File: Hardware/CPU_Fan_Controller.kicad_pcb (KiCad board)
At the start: 2 copper layers, 45.5 x 10.8 mm, 14 parts, among them J1 Conn_01x05_Pin, J2 Conn_01x04_Socket, J3 Conn_01x01_Socket, J4 Conn_01x01_Socket, SW1 SW_Push, U1 STM32G030J6Mx, U2 LD1117S33TR_SOT223

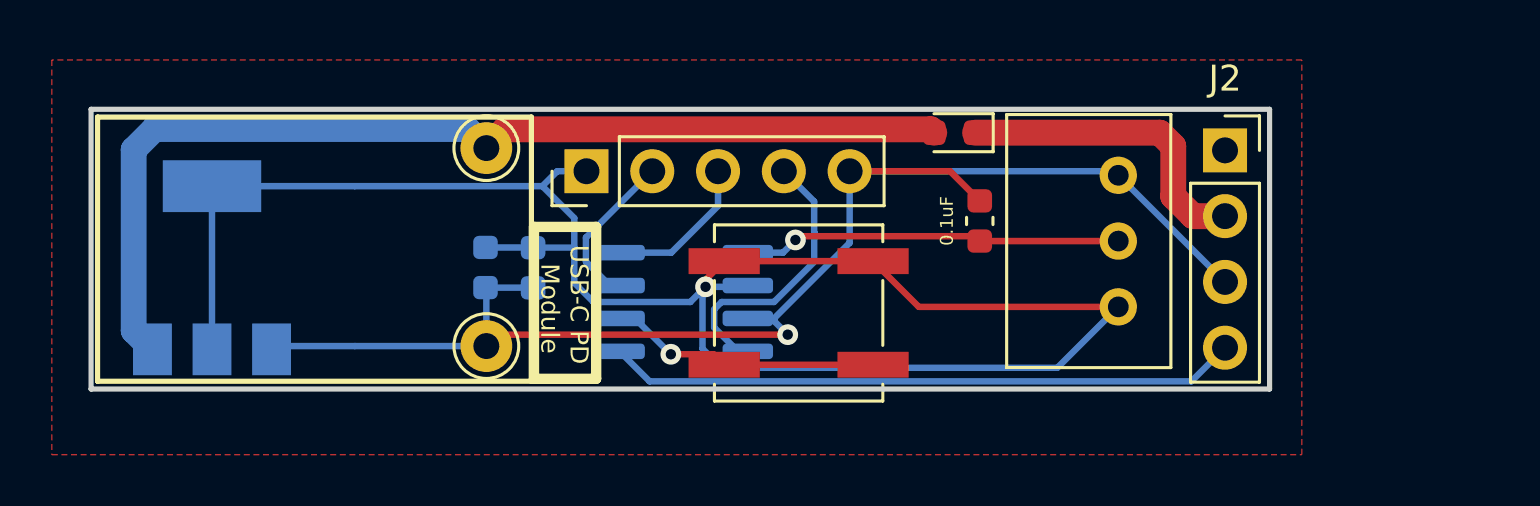
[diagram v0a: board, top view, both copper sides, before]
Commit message: Code is functioning, updated PCB
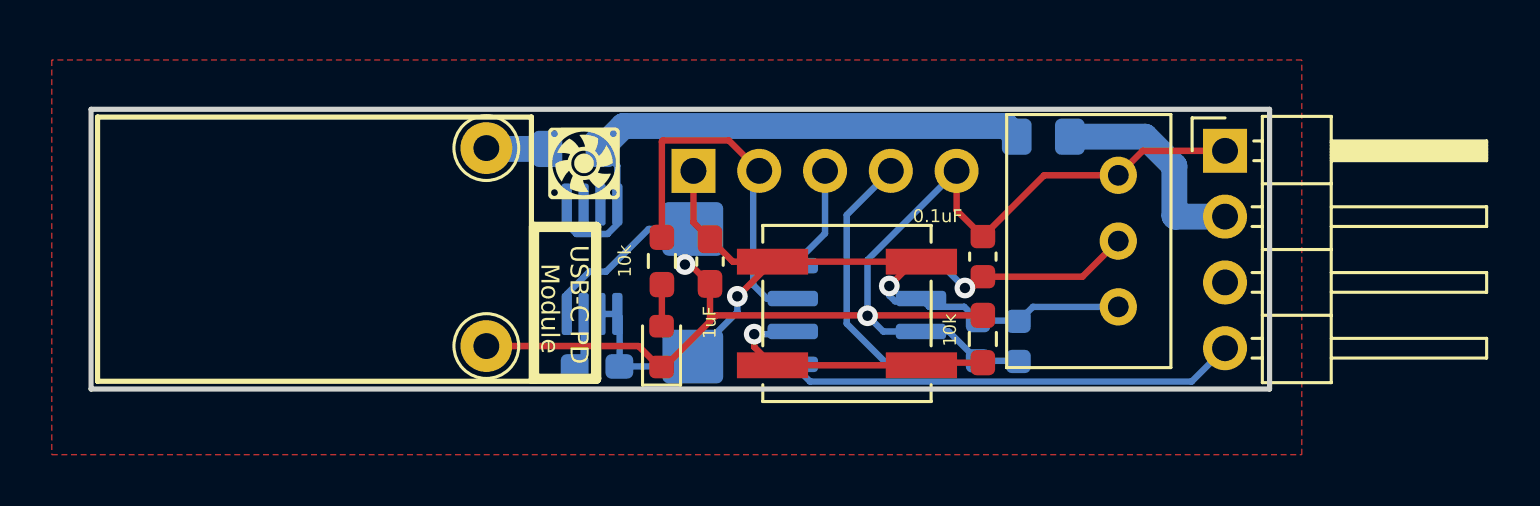
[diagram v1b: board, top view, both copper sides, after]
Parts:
- removed J2: Conn_01x04_Socket, Connector_PinSocket_2.54mm:PinSocket_1x04_P2.54mm_Vertical
- added C4: 1uF, Capacitor_SMD:C_0603_1608Metric_Pad1.08x0.95mm_HandSolder, F.Cu at (183.9, 89.9)
- added C5: 0.01uF, Capacitor_SMD:C_0603_1608Metric_Pad1.08x0.95mm_HandSolder, B.Cu at (179.5, 93.9)
- added C6: 10uF, Capacitor_Tantalum_SMD:CP_EIA-6032-15_Kemet-U, B.Cu at (183.2, 91.1)
- added D2: LED, LED_SMD:LED_0603_1608Metric, F.Cu at (182.0, 93.2)
- added D3: D_Schottky, Diode_SMD:D_0805_2012Metric_Pad1.15x1.40mm_HandSolder, B.Cu at (178.6, 85.5)
- added M1: Fan_CPU_4pin, Connector_PinHeader_2.54mm:PinHeader_1x04_P2.54mm_Horizontal, F.Cu at (203.8, 85.6)
- added R1: 10k, Resistor_SMD:R_0603_1608Metric_Pad0.98x0.95mm_HandSolder, F.Cu at (194.4, 92.9)
- added R2: 10k, Resistor_SMD:R_0603_1608Metric_Pad0.98x0.95mm_HandSolder, F.Cu at (182.0, 89.9)
- D1: footprint Diode_SMD:D_0603_1608Metric -> Diode_SMD:D_0805_2012Metric_Pad1.15x1.40mm_HandSolder; moved to B.Cu
- G***: moved to F.Cu
- RV1: value R_Potentiometer -> 10kohm
- U2: value LD1117S33TR_SOT223 -> LT1962-3.3; footprint Package_TO_SOT_SMD:SOT-223-3_TabPin2 -> Package_SO:MSOP-8_3x3mm_P0.65mm
- moved G*** 26.3 mm to (167.2, 91.3)
- moved C2 20.8 mm to (195.8, 93.0)
- moved C3 17.4 mm to (194.2, 92.9)
- moved U2 14.7 mm to (179.3, 89.8)
- moved G*** 9.34 mm to (179.0, 86.1), turned to 0 degrees
- moved U1 6.70 mm to (189.6, 91.9)
- moved J1 4.13 mm to (183.3, 86.4)
- moved D1 3.43 mm to (196.8, 85.1)
- moved SW1 1.87 mm to (189.2, 91.9)
- moved C1 1.38 mm to (194.4, 89.7)
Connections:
- net Net-(U1-PA12/PA10) renamed BUTTON
- net Net-(U1-PC14/PB7/PB8/PB9) renamed POT_ADC
- J4 pad 1: +12V -> Net-(D3-A)
- U2 pad 1: GND -> +3.3V
- U2 pad 3: +12V -> Net-(U2-BYP)
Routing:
- net +3.3V: track 72.9 -> 33.5 mm, vias 1 -> 2
- net +12V: track 39.9 -> 22.1 mm
- net SWDIO: track 6.23 -> 14.2 mm
- net PWM: track 24.4 -> 17.5 mm
- net POT_ADC: track 14.7 -> 8.73 mm
- net GND: track 54.7 -> 59.2 mm, vias 1 -> 2
- net Net-(D1-K): track 12.1 -> 8.40 mm
- net Net-(D3-A): track 0.00 -> 2.32 mm
- net Net-(U2-BYP): track 0.00 -> 2.17 mm
- net SWCLK: track 5.89 -> 4.18 mm
- net Net-(D2-A): track 0.00 -> 1.52 mm
- net NRST: track 11.0 -> 10.1 mm
- net BUTTON: track 10.5 -> 11.2 mm
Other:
- board text added: "3.3v LDO"
- board text added: "CPU FAN SPEED CONTROLLER V2.0 Joseph Douglas 8/24/2023"
- board text added: "STM32G030"
- board text removed: "12v to 3.3v LDO"
- board text removed: "CPU FAN SPEED CONTROLLER V1.0 Joseph Douglas 7/18/2023"
- board text removed: "STM32G030J6"
